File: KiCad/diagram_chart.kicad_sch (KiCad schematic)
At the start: 15 parts, among them J1 Barrel_Jack, J2 Screw_Terminal_01x02, SW1 SW_SPDT, U2 74HC165

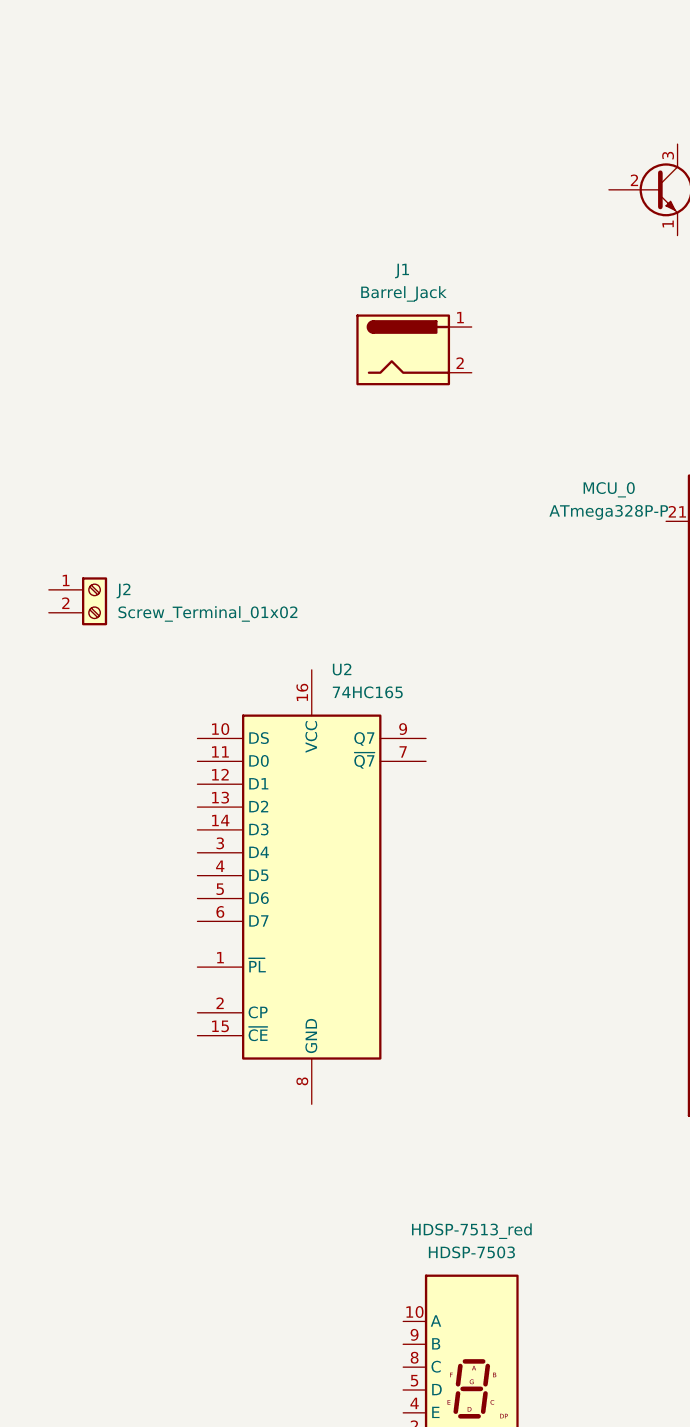
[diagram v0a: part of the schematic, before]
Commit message: Restructured some and decided to go with 8mm char height
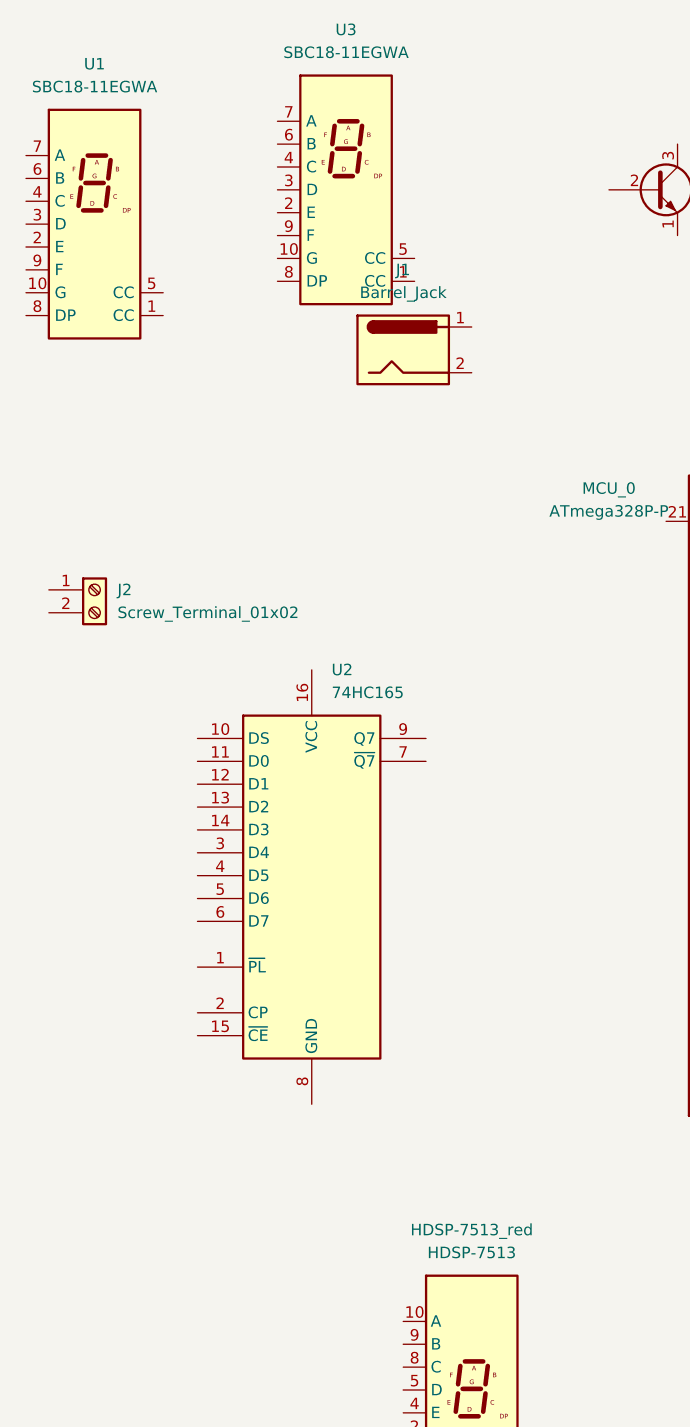
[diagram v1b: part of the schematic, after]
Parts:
- added U1, U3: SBC18-11EGWA, Display_7Segment:SBC18-11SURKCGKWA, symbol Display_Character:SBC18-11EGWA
- HDSP-7513_red: value HDSP-7503 -> HDSP-7513; footprint Display_7Segment:HDSP-A151 -> Display_7Segment:HDSP-7507
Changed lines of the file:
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@@
+    )
+  )
+  (symbol (lib_id "Display_Character:SBC18-11EGWA") (at 46.99 41.91 0) (unit 1)
+    (in_bom yes) (on_board yes) (dnp no) (fields_autoplaced)
+    (property "Reference" "U1" (at 46.99 24.13 0)
+      (effects (font (size 1.27 1.27)))
+    )
+    (property "Value" "SBC18-11EGWA" (at 46.99 26.67 0)
+      (effects (font (size 1.27 1.27)))
+    )
+    (property "Footprint" "Display_7Segment:SBC18-11SURKCGKWA" (at 28.448 59.944 0)
+      (effects (font (size 1.27 1.27)) (justify left) hide)
+    )
+    (property "Datasheet" "http://www.kingbrightusa.com/images/catalog/SPEC/SBC18-11EGWA.pdf" (at 46.99 37.084 0)
+      (effects (font (size 1.27 1.27)) (justify left) hide)
+    )
+    (pin "2")
+    (pin "1")
+    (pin "9")
+    (pin "3")
+    (pin "5")
+    (pin "7")
+    (pin "10")
+    (pin "4")
+    (pin "8")
+    (pin "6")
+    (instances
+      (project "diagram_chart"
+        (path "/6dfb841c-0ebb-4587-a5cf-7b85233b045b"
+          (reference "U1") (unit 1)
+        )
+      )
     )
   )
@@
     )
   )
+  (symbol (lib_id "Display_Character:SBC18-11EGWA") (at 74.93 38.1 0) (unit 1)
+    (in_bom yes) (on_board yes) (dnp no) (fields_autoplaced)
+    (property "Reference" "U3" (at 74.93 20.32 0)
+      (effects (font (size 1.27 1.27)))
+    )
+    (property "Value" "SBC18-11EGWA" (at 74.93 22.86 0)
+      (effects (font (size 1.27 1.27)))
+    )
+    (property "Footprint" "Display_7Segment:SBC18-11SURKCGKWA" (at 56.388 56.134 0)
+      (effects (font (size 1.27 1.27)) (justify left) hide)
+    )
+    (property "Datasheet" "http://www.kingbrightusa.com/images/catalog/SPEC/SBC18-11EGWA.pdf" (at 74.93 33.274 0)
+      (effects (font (size 1.27 1.27)) (justify left) hide)
+    )
+    (pin "10")
+    (pin "3")
+    (pin "4")
+    (pin "9")
+    (pin "1")
+    (pin "6")
+    (pin "8")
+    (pin "7")
+    (pin "5")
+    (pin "2")
+    (instances
+      (project "diagram_chart"
+        (path "/6dfb841c-0ebb-4587-a5cf-7b85233b045b"
+          (reference "U3") (unit 1)
+        )
+      )
+    )
+  )
   (symbol (lib_id "Transistor_BJT:2N3904") (at 153.67 57.15 0) (unit 1)
     (in_bom yes) (on_board yes) (dnp no) (fields_autoplaced)
@@
       (effects (font (size 1.27 1.27)))
     )
-    (property "Value" "HDSP-7503" (at 88.9 156.21 0)
-      (effects (font (size 1.27 1.27)))
-    )
-    (property "Footprint" "Display_7Segment:HDSP-A151" (at 88.9 185.42 0)
-      (effects (font (size 1.27 1.27)) hide)
-    )
+    (property "Value" "HDSP-7513" (at 88.9 156.21 0)
+      (effects (font (size 1.27 1.27)))
+    )
+    (property "Footprint" "Display_7Segment:HDSP-7507" (at 88.9 185.42 0)
+      (effects (font (size 1.27 1.27)) hide)
+    )

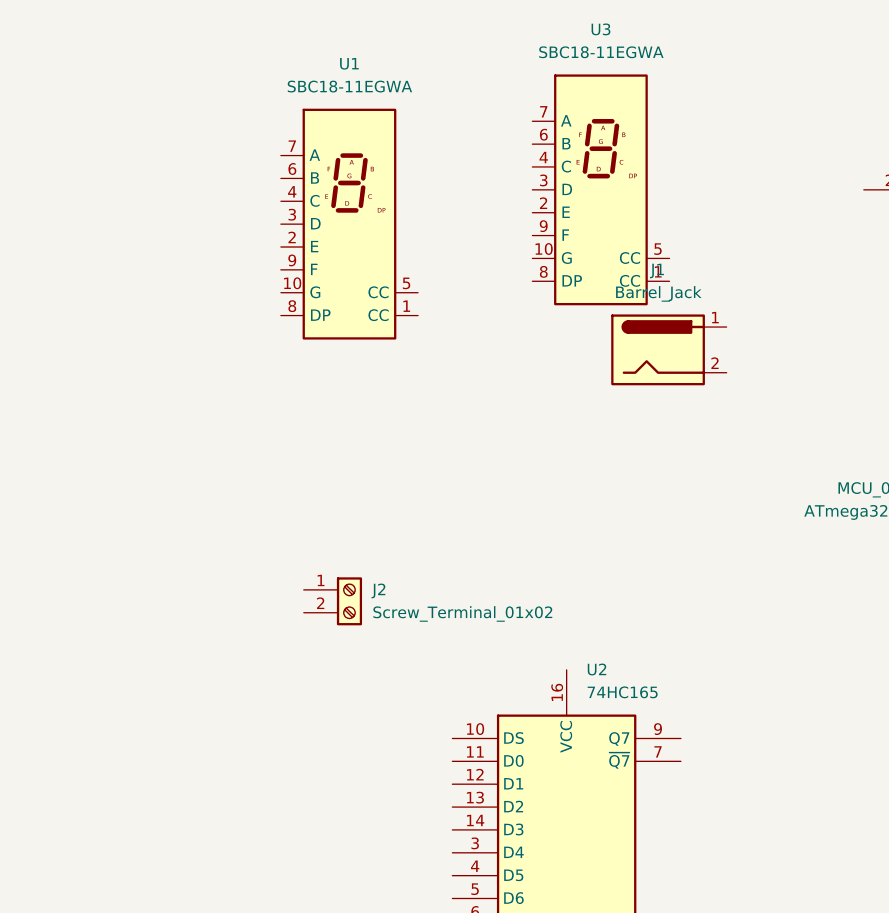
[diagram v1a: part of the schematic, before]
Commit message: Addewd new barrel-jack and added 14mm 7-segment
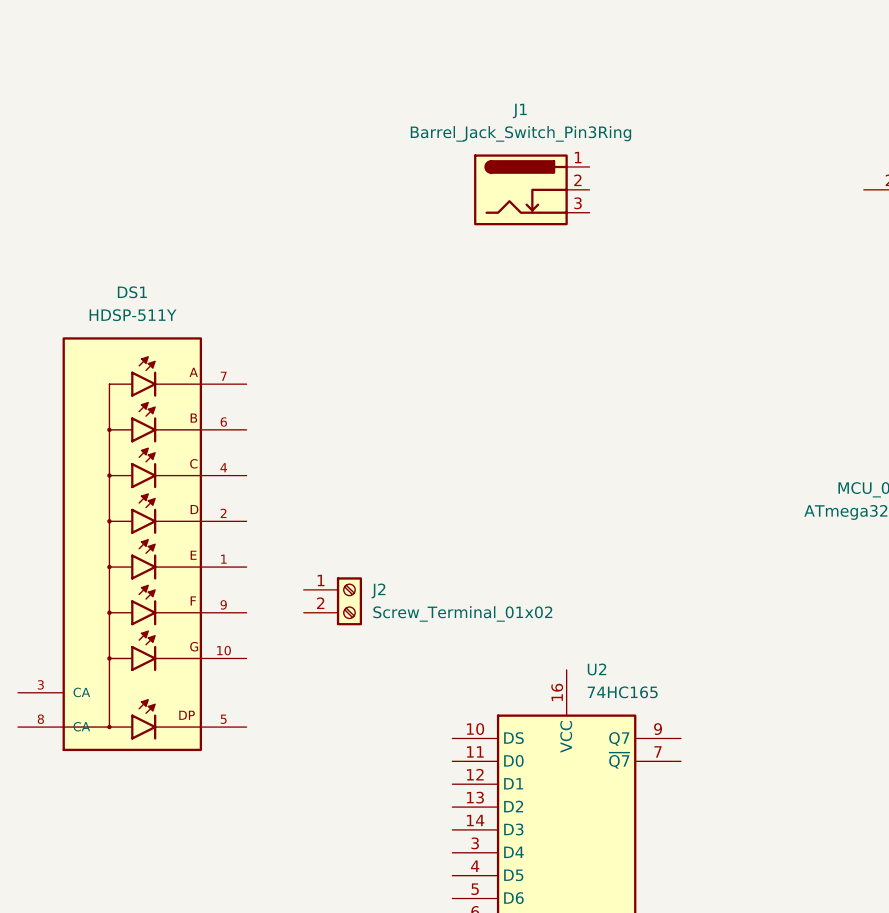
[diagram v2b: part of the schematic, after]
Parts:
- removed J1: Barrel_Jack, Connector_BarrelJack:BarrelJack_CUI_PJ-102AH_Horizontal, symbol Connector:Barrel_Jack
- removed U1, U3: SBC18-11EGWA, Display_7Segment:SBC18-11SURKCGKWA, symbol Display_Character:SBC18-11EGWA
- added DS1: HDSP-511Y, HDSP-511Y:LED_HDSP-511Y, symbol HDSP-511Y:HDSP-511Y
- added J1: Barrel_Jack_Switch_Pin3Ring, dc-barrelljacks:BarrelJack_CUI_PJ-102AH_Horizontal, symbol Connector:Barrel_Jack_Switch_Pin3Ring
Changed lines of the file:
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@@
-    )
-  )
-  (symbol (lib_id "Connector:Barrel_Jack") (at 81.28 55.88 0) (unit 1)
-    (in_bom yes) (on_board yes) (dnp no) (fields_autoplaced)
-    (property "Reference" "J1" (at 81.28 46.99 0)
-      (effects (font (size 1.27 1.27)))
-    )
-    (property "Value" "Barrel_Jack" (at 81.28 49.53 0)
-      (effects (font (size 1.27 1.27)))
-    )
-    (property "Footprint" "Connector_BarrelJack:BarrelJack_CUI_PJ-102AH_Horizontal" (at 82.55 56.896 0)
-      (effects (font (size 1.27 1.27)) hide)
-    )
-    (property "Datasheet" "~" (at 82.55 56.896 0)
-      (effects (font (size 1.27 1.27)) hide)
-    )
-    (pin "1")
-    (pin "2")
-    (instances
-      (project "diagram_chart"
-        (path "/6dfb841c-0ebb-4587-a5cf-7b85233b045b"
-          (reference "J1") (unit 1)
-        )
-      )
     )
   )
@@
     )
   )
-  (symbol (lib_id "Display_Character:SBC18-11EGWA") (at 46.99 41.91 0) (unit 1)
-    (in_bom yes) (on_board yes) (dnp no) (fields_autoplaced)
-    (property "Reference" "U1" (at 46.99 24.13 0)
-      (effects (font (size 1.27 1.27)))
-    )
-    (property "Value" "SBC18-11EGWA" (at 46.99 26.67 0)
-      (effects (font (size 1.27 1.27)))
-    )
-    (property "Footprint" "Display_7Segment:SBC18-11SURKCGKWA" (at 28.448 59.944 0)
-      (effects (font (size 1.27 1.27)) (justify left) hide)
-    )
-    (property "Datasheet" "http://www.kingbrightusa.com/images/catalog/SPEC/SBC18-11EGWA.pdf" (at 46.99 37.084 0)
-      (effects (font (size 1.27 1.27)) (justify left) hide)
-    )
-    (pin "2")
-    (pin "1")
-    (pin "9")
-    (pin "3")
-    (pin "5")
-    (pin "7")
-    (pin "10")
-    (pin "4")
-    (pin "8")
-    (pin "6")
-    (instances
-      (project "diagram_chart"
-        (path "/6dfb841c-0ebb-4587-a5cf-7b85233b045b"
-          (reference "U1") (unit 1)
-        )
-      )
-    )
-  )
   (symbol (lib_id "Interface_Expansion:TPIC6595") (at 223.52 116.84 0) (unit 1)
     (in_bom yes) (on_board yes) (dnp no) (fields_autoplaced)
@@
     )
   )
-  (symbol (lib_id "Display_Character:SBC18-11EGWA") (at 74.93 38.1 0) (unit 1)
-    (in_bom yes) (on_board yes) (dnp no) (fields_autoplaced)
-    (property "Reference" "U3" (at 74.93 20.32 0)
-      (effects (font (size 1.27 1.27)))
-    )
-    (property "Value" "SBC18-11EGWA" (at 74.93 22.86 0)
-      (effects (font (size 1.27 1.27)))
-    )
-    (property "Footprint" "Display_7Segment:SBC18-11SURKCGKWA" (at 56.388 56.134 0)
-      (effects (font (size 1.27 1.27)) (justify left) hide)
-    )
-    (property "Datasheet" "http://www.kingbrightusa.com/images/catalog/SPEC/SBC18-11EGWA.pdf" (at 74.93 33.274 0)
-      (effects (font (size 1.27 1.27)) (justify left) hide)
-    )
+  (symbol (lib_id "Connector:Barrel_Jack_Switch_Pin3Ring") (at 66.04 38.1 0) (unit 1)
+    (in_bom yes) (on_board yes) (dnp no) (fields_autoplaced)
+    (property "Reference" "J1" (at 66.04 29.21 0)
+      (effects (font (size 1.27 1.27)))
+    )
+    (property "Value" "Barrel_Jack_Switch_Pin3Ring" (at 66.04 31.75 0)
+      (effects (font (size 1.27 1.27)))
+    )
+    (property "Footprint" "dc-barrelljacks:BarrelJack_CUI_PJ-102AH_Horizontal" (at 67.31 39.116 0)
+      (effects (font (size 1.27 1.27)) hide)
+    )
+    (property "Datasheet" "~" (at 67.31 39.116 0)
+      (effects (font (size 1.27 1.27)) hide)
+    )
+    (pin "1")
+    (pin "3")
+    (pin "2")
+    (instances
+      (project "diagram_chart"
+        (path "/6dfb841c-0ebb-4587-a5cf-7b85233b045b"
+          (reference "J1") (unit 1)
+        )
+      )
+    )
+  )
+  (symbol (lib_id "Transistor_BJT:2N3904") (at 153.67 57.15 0) (unit 1)
+    (in_bom yes) (on_board yes) (dnp no) (fields_autoplaced)
+    (property "Reference" "T_DEC_1" (at 158.75 55.88 0)
+      (effects (font (size 1.27 1.27)) (justify left))
+    )
+    (property "Value" "2N3904" (at 158.75 58.42 0)
+      (effects (font (size 1.27 1.27)) (justify left))
+    )
+    (property "Footprint" "Package_TO_SOT_THT:TO-92_Inline" (at 158.75 59.055 0)
+      (effects (font (size 1.27 1.27) italic) (justify left) hide)
+    )
+    (property "Datasheet" "https://www.onsemi.com/pub/Collateral/2N3903-D.PDF" (at 153.67 57.15 0)
+      (effects (font (size 1.27 1.27)) (justify left) hide)
+    )
+    (pin "3")
+    (pin "1")
+    (pin "2")
+    (instances
+      (project "diagram_chart"
+        (path "/6dfb841c-0ebb-4587-a5cf-7b85233b045b"
+          (reference "T_DEC_1") (unit 1)
+        )
+      )
+    )
+  )
+  (symbol (lib_id "HDSP-511Y:HDSP-511Y") (at 22.86 77.47 0) (unit 1)
+    (in_bom yes) (on_board yes) (dnp no) (fields_autoplaced)
+    (property "Reference" "DS1" (at 22.86 49.53 0)
+      (effects (font (size 1.27 1.27)))
+    )
+    (property "Value" "HDSP-511Y" (at 22.86 52.07 0)
+      (effects (font (size 1.27 1.27)))
+    )
+    (property "Footprint" "HDSP-511Y:LED_HDSP-511Y" (at 22.86 77.47 0)
+      (effects (font (size 1.27 1.27)) (justify bottom) hide)
+    )
+    (property "Datasheet" "" (at 22.86 77.47 0)
+      (effects (font (size 1.27 1.27)) hide)
+    )
+    (property "MF" "Broadcom Limited" (at 22.86 77.47 0)
+      (effects (font (size 1.27 1.27)) (justify bottom) hide)
+    )
+    (property "MAXIMUM_PACKAGE_HEIGHT" "8.00mm" (at 22.86 77.47 0)
+      (effects (font (size 1.27 1.27)) (justify bottom) hide)
+    )
+    (property "Package" "None" (at 22.86 77.47 0)
+      (effects (font (size 1.27 1.27)) (justify bottom) hide)
+    )
+    (property "Price" "None" (at 22.86 77.47 0)
+      (effects (font (size 1.27 1.27)) (justify bottom) hide)
+    )
+    (property "Check_prices" "https://www.snapeda.com/parts/HDSP-511Y/Broadcom+Limited/view-part/?ref=eda" (at 22.86 77.47 0)
+      (effects (font (size 1.27 1.27)) (justify bottom) hide)
+    )
+    (property "STANDARD" "Manufacturer Recommendations" (at 22.86 77.47 0)
+      (effects (font (size 1.27 1.27)) (justify bottom) hide)
+    )
+    (property "PARTREV" "April 12, 2021" (at 22.86 77.47 0)
+      (effects (font (size 1.27 1.27)) (justify bottom) hide)
+    )
+    (property "SnapEDA_Link" "https://www.snapeda.com/parts/HDSP-511Y/Broadcom+Limited/view-part/?ref=snap" (at 22.86 77.47 0)
+      (effects (font (size 1.27 1.27)) (justify bottom) hide)
+    )
+    (property "MP" "HDSP-511Y" (at 22.86 77.47 0)
+      (effects (font (size 1.27 1.27)) (justify bottom) hide)
+    )
+    (property "Purchase-URL" "https://www.snapeda.com/api/url_track_click_mouser/?unipart_id=267845&manufacturer=Broadcom Limited&part_name=HDSP-511Y&search_term=None" (at 22.86 77.47 0)
+      (effects (font (size 1.27 1.27)) (justify bottom) hide)
+    )
+    (property "Description" "\nDisplay Modules - LED Character and Numeric Yellow 7-Segment 1 Character Common Anode 2.15V 20mA 0.673 H x 0.488 W x 0.315 D (17.10mm x 12.40mm x 8.00mm) 10-DIP (0.600, 15.24mm)\n" (at 22.86 77.47 0)
+      (effects (font (size 1.27 1.27)) (justify bottom) hide)
+    )
+    (property "Availability" "In Stock" (at 22.86 77.47 0)
+      (effects (font (size 1.27 1.27)) (justify bottom) hide)
+    )
+    (property "MANUFACTURER" "Broadcom" (at 22.86 77.47 0)
+      (effects (font (size 1.27 1.27)) (justify bottom) hide)
+    )
+    (pin "3")
+    (pin "7")
+    (pin "8")
     (pin "10")
-    (pin "3")
+    (pin "2")
     (pin "4")
+    (pin "1")
+    (pin "6")
     (pin "9")
-    (pin "1")
-    (pin "6")
-    (pin "8")
-    (pin "7")
     (pin "5")
-    (pin "2")
-    (instances
-      (project "diagram_chart"
-        (path "/6dfb841c-0ebb-4587-a5cf-7b85233b045b"
-          (reference "U3") (unit 1)
-        )
-      )
-    )
-  )
-  (symbol (lib_id "Transistor_BJT:2N3904") (at 153.67 57.15 0) (unit 1)
-    (in_bom yes) (on_board yes) (dnp no) (fields_autoplaced)
-    (property "Reference" "T_DEC_1" (at 158.75 55.88 0)
-      (effects (font (size 1.27 1.27)) (justify left))
-    )
-    (property "Value" "2N3904" (at 158.75 58.42 0)
-      (effects (font (size 1.27 1.27)) (justify left))
-    )
-    (property "Footprint" "Package_TO_SOT_THT:TO-92_Inline" (at 158.75 59.055 0)
-      (effects (font (size 1.27 1.27) italic) (justify left) hide)
-    )
-    (property "Datasheet" "https://www.onsemi.com/pub/Collateral/2N3903-D.PDF" (at 153.67 57.15 0)
-      (effects (font (size 1.27 1.27)) (justify left) hide)
-    )
-    (pin "3")
-    (pin "1")
-    (pin "2")
-    (instances
-      (project "diagram_chart"
-        (path "/6dfb841c-0ebb-4587-a5cf-7b85233b045b"
-          (reference "T_DEC_1") (unit 1)
-        )
-      )
+    (instances
+      (project "diagram_chart"
+        (path "/6dfb841c-0ebb-4587-a5cf-7b85233b045b"
+          (reference "DS1") (unit 1)
+        )
+      )

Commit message: Halfway done with wire-diagram, 90% of components have footprints
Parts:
- removed HDSP-7513_red: HDSP-7513, Display_7Segment:HDSP-7507, symbol Display_Character:HDSP-7503
- removed HDSP-7803_green: HDSP-7503, Display_7Segment:HDSP-A151, symbol Display_Character:HDSP-7503
- added D0, D1, D2, D3, D4, D5, D6, D7: LED, LED_THT:LED_D5.0mm, symbol Device:LED
- added R0, R1, R2, R3, R4, R5, R6, R7: 220Ω, Resistor_THT:R_Axial_DIN0207_L6.3mm_D2.5mm_P7.62mm_Horizontal, symbol Device:R
- added R8: 10kΩ, Resistor_THT:R_Axial_DIN0204_L3.6mm_D1.6mm_P5.08mm_Horizontal, symbol Device:R
- added decimal_0, decimal_1, decimal_2, hex_1: HDSP-511Y, HDSP-511Y:LED_HDSP-511Y, symbol HDSP-511Y:HDSP-511Y
- renumbered SW1 to SW0, DS1 to hex_0
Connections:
- net at SW0.2 (B): now also U2.11 (D0), R8.1
- net at U_Out.14 (DRAIN4): now also R4.2
- net at U_Out.15 (DRAIN5): now also R5.2
- net at U_Out.16 (DRAIN6): now also R6.2
- net at U_Out.17 (DRAIN7): now also R7.2
- net at U_Out.4 (DRAIN0): now also R0.2
- net at U_Out.5 (DRAIN1): now also R1.2
- net at U_Out.6 (DRAIN2): now also R2.2
- net at U_Out.7 (DRAIN3): now also R3.2
- net at hex_0.1: now also D4.1 (K), R4.1, decimal_0.1, decimal_1.1, decimal_2.1, hex_1.1
- net at hex_0.10: now also D6.1 (K), R6.1, decimal_0.10, decimal_1.10, decimal_2.10, hex_1.10
- net at hex_0.2: now also D3.1 (K), R3.1, decimal_0.2, decimal_1.2, decimal_2.2, hex_1.2
- net at hex_0.4: now also D2.1 (K), R2.1, decimal_0.4, decimal_1.4, decimal_2.4, hex_1.4
- net at hex_0.5: now also D7.1 (K), R7.1, decimal_0.5, decimal_1.5, decimal_2.5, hex_1.5
- net at hex_0.6: now also D1.1 (K), R1.1, decimal_0.6, decimal_1.6, decimal_2.6, hex_1.6
- net at hex_0.7: now also D0.1 (K), R0.1, decimal_0.7, decimal_1.7, decimal_2.7, hex_1.7
- net at hex_0.9: now also D5.1 (K), R5.1, decimal_0.9, decimal_1.9, decimal_2.9, hex_1.9
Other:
- moved on the sheet: J1, J2, MCU_0, SW0, T_DEC_0, T_DEC_1, T_DEC_2, T_HEX_0, T_HEX_1, T_LED, U2, U_Caps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
